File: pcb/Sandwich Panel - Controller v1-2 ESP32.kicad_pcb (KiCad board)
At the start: 2 copper layers, 140 x 50 mm, 28 parts, among them J1 Conn_01x02_Male, J2 Conn_01x02_Male, J4 Conn_01x04, J5 USB_C_Receptacle_USB2.0, U1 ESP32-S3-MINI-1-N8, U2 SPX3819M5-L-3-3

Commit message: Old zones don't seem to be removable, will edit the text file next, wish me luck
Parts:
- removed H4, H5, H6, H7, H8: Mousebites, Pancake:Mousebites_03
- removed J1, J2: Conn_01x02_Male, Pancake:Panel_Connector 02
- removed J4: Conn_01x04, Pancake:I2C Breakout Pads
- added H3: Mousebites, Pancake:Mousebites_03, F.Cu at (33.5, 64.8)
- added H3: Mousebites, Pancake:Mousebites_03, F.Cu at (153.0, 95.2)
- added H3: Mousebites, Pancake:Mousebites_03, F.Cu at (35.0, 144.2)
- added H3: Mousebites, Pancake:Mousebites_03, F.Cu at (153.0, 50.2)
- added H3: Mousebites, Pancake:Mousebites_03, F.Cu at (152.0, 144.2)
- added H3: Mousebites, Pancake:Mousebites_03, F.Cu at (152.0, 116.8)
- added H3: Mousebites, Pancake:Mousebites_03, F.Cu at (34.0, 116.2)
- added H3: Mousebites, Pancake:Mousebites_03, F.Cu at (33.5, 95.8)
- added H3: Mousebites, Pancake:Mousebites_03, F.Cu at (153.0, 64.8)
- added H3: Mousebites, Pancake:Mousebites_03, F.Cu at (151.5, 80.2)
- added H3: Mousebites, Pancake:Mousebites_03, F.Cu at (34.0, 80.8)
- moved H1 220.5 mm to (157.5, 45.0)
- moved H3 117.6 mm to (33.5, 50.2)
- moved U1 114.6 mm to (138.9, 34.0)
- moved TP2 111.9 mm to (135.0, 43.0)
- moved TP3 111.9 mm to (136.5, 43.0)
- moved TP4 111.9 mm to (138.0, 43.0)
- moved TP5 111.9 mm to (139.5, 43.0)
- moved TP6 111.9 mm to (141.0, 43.0)
- moved TP7 111.9 mm to (142.5, 43.0)
- moved C1 110.9 mm to (122.5, 30.0)
- moved C2 110.9 mm to (122.5, 38.7)
- moved C3 110.9 mm to (118.0, 34.4)
- moved R3 110.9 mm to (117.9, 30.1)
- moved TP1 110.9 mm to (126.0, 31.6)
- moved U2 110.9 mm to (122.5, 34.4)
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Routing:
- net +5V: track 133.6 -> 0.00 mm, vias 6 -> 2
- net 3.3V: track 110.3 -> 0.00 mm
- net SDA: track 100.8 -> 0.00 mm, vias 2 -> 1
- net SCL: track 98.8 -> 0.00 mm, vias 2 -> 1
- net Net-(H1-Pad1): track 95.7 -> 0.00 mm
- net Net-(H2-Pad1): track 36.8 -> 0.00 mm
- net D-: track 36.6 -> 0.00 mm
- net D+: track 34.7 -> 0.00 mm
- net Net-(C3-Pad1): track 30.2 -> 0.00 mm
- net DOUT: track 24.8 -> 0.00 mm, vias 2 -> 0
- net GND: track 16.0 -> 0.00 mm, vias 9 -> 4
- net Net-(J5-PadA5): track 11.1 -> 0.00 mm
- net Net-(J5-PadB5): track 7.37 -> 0.00 mm
- net Net-(U1-Pad26): track 4.77 -> 0.00 mm
- net Net-(U1-Pad30): track 4.62 -> 0.00 mm
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- added copper zone on F.Cu, net +5V
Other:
- board size 140 x 50 mm -> 140.5 x 160.6 mm
- board text added: "Controller v1-4"
- board text added: "PancakeLegend et al 2024"
- board text removed: "Controller v1-3"
- board text removed: "JLCJLCJLCJLC"
- board text removed: "PancakeLegend 2023"

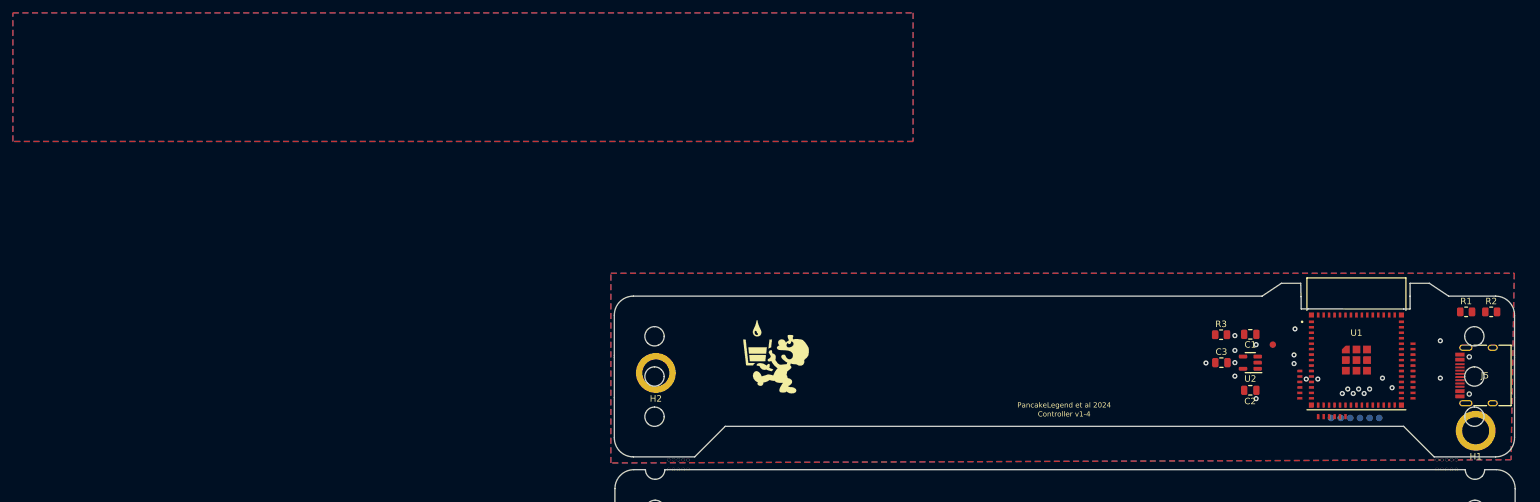
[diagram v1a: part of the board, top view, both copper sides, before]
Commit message: Successful removal of stray zones (manually)
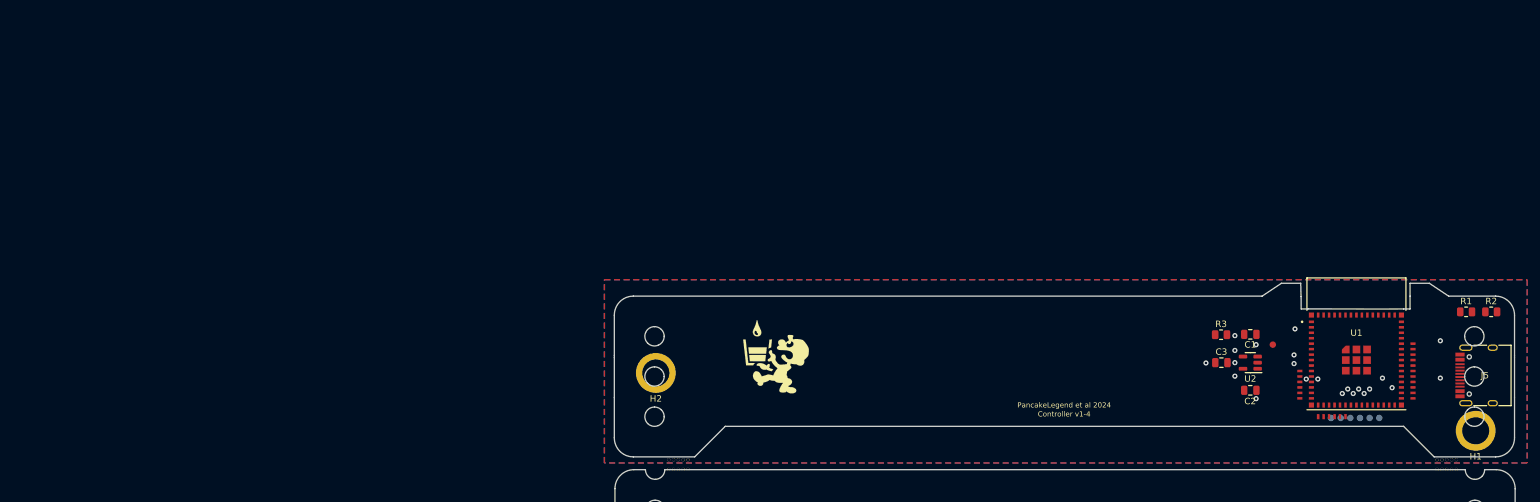
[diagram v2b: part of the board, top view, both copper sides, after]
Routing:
- removed copper zone on F.Cu, net GND
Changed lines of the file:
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@@
 			(pinfunction "GND")
 			(pintype "power_in")
-			(zone_connect 0)
 			(options
 				(clearance outline)
@@
 			(pintype "power_in")
 		)
-		(zone
-			(net 0)
-			(net_name "")
-			(layer "F.Cu")
-			(hatch full 0.508)
-			(connect_pads
-				(clearance 0)
-			)
-			(min_thickness 0.01)
-			(filled_areas_thickness no)
-			(keepout
-				(tracks not_allowed)
-				(vias not_allowed)
-				(pads not_allowed)
-				(copperpour not_allowed)
-				(footprints allowed)
-			)
-			(fill
-				(thermal_gap 0.508)
-				(thermal_bridge_width 0.508)
-			)
-			(polygon
-				(pts
-					(xy 131.25 21.225) (xy 146.65 21.225) (xy 146.65 26.275) (xy 131.25 26.275)
-				)
-			)
-		)
-		(zone
-			(net 0)
-			(net_name "")
-			(layers "*.Cu")
-			(hatch full 0.508)
-			(connect_pads
-				(clearance 0)
-			)
-			(min_thickness 0.01)
-			(filled_areas_thickness no)
-			(keepout
-				(tracks allowed)
-				(vias not_allowed)
-				(pads allowed)
-				(copperpour allowed)
-				(footprints allowed)
-			)
-			(fill
-				(thermal_gap 0.508)
-				(thermal_bridge_width 0.508)
-			)
-			(polygon
-				(pts
-					(xy 131.25 21.225) (xy 146.65 21.225) (xy 146.65 26.275) (xy 131.25 26.275)
-				)
-			)
-		)
-		(zone
-			(net 0)
-			(net_name "")
-			(layer "B.Cu")
-			(hatch full 0.508)
-			(connect_pads
-				(clearance 0)
-			)
-			(min_thickness 0.01)
-			(filled_areas_thickness no)
-			(keepout
-				(tracks not_allowed)
-				(vias not_allowed)
-				(pads not_allowed)
-				(copperpour not_allowed)
-				(footprints allowed)
-			)
-			(fill
-				(thermal_gap 0.508)
-				(thermal_bridge_width 0.508)
-			)
-			(polygon
-				(pts
-					(xy 131.25 21.225) (xy 146.65 21.225) (xy 146.65 26.275) (xy 131.25 26.275)
-				)
-			)
-		)
 		(model "C:/Users/ocd/OneDrive/KiCAD/3D Models/ESP32-S3-MINI-1-N8.step"
 			(offset
@@
 	)
 	(zone
-		(net 1)
-		(net_name "GND")
-		(locked yes)
-		(layer "F.Cu")
-		(hatch edge 0.508)
-		(connect_pads
-			(clearance 0.5)
-		)
-		(min_thickness 0.254)
-		(filled_areas_thickness no)
-		(fill yes
-			(thermal_gap 0.508)
-			(thermal_bridge_width 0.508)
-		)
-		(polygon
-			(pts
-				(xy 70 0) (xy -70 0) (xy -70 -20) (xy 70 -20)
-			)
-		)
-	)
-	(zone
 		(net 4)
 		(net_name "+5V")
 		(layer "F.Cu")
 		(hatch edge 0.5)
-		(priority 1)
 		(connect_pads
 			(clearance 0)
@@
 		(polygon
 			(pts
-				(xy 23 20.5) (xy 163.5 20.5) (xy 163 49.5) (xy 23 50)
+				(xy 165.5 21.5) (xy 165.5 50) (xy 22 50) (xy 22 21.5)
 			)
 		)
@@
 		(layer "B.Cu")
 		(hatch edge 0.5)
-		(priority 2)
 		(connect_pads
 			(clearance 0)
@@
 		(polygon
 			(pts
-				(xy 23 20.5) (xy 163.5 20.5) (xy 163 49.5) (xy 23 50)
-			)
-		)
-	)
-	(zone
-		(net 1)
-		(net_name "GND")
-		(locked yes)
-		(layer "B.Cu")
-		(hatch edge 0.508)
-		(connect_pads
-			(clearance 0.5)
-		)
-		(min_thickness 0.254)
-		(filled_areas_thickness no)
-		(fill yes
-			(thermal_gap 0.508)
-			(thermal_bridge_width 0.508)
-		)
-		(polygon
-			(pts
-				(xy 70 0) (xy -70 0) (xy -70 -20) (xy 70 -20)
+				(xy 165.5 21.5) (xy 165.5 50) (xy 22 50) (xy 22 21.5)
 			)
 		)

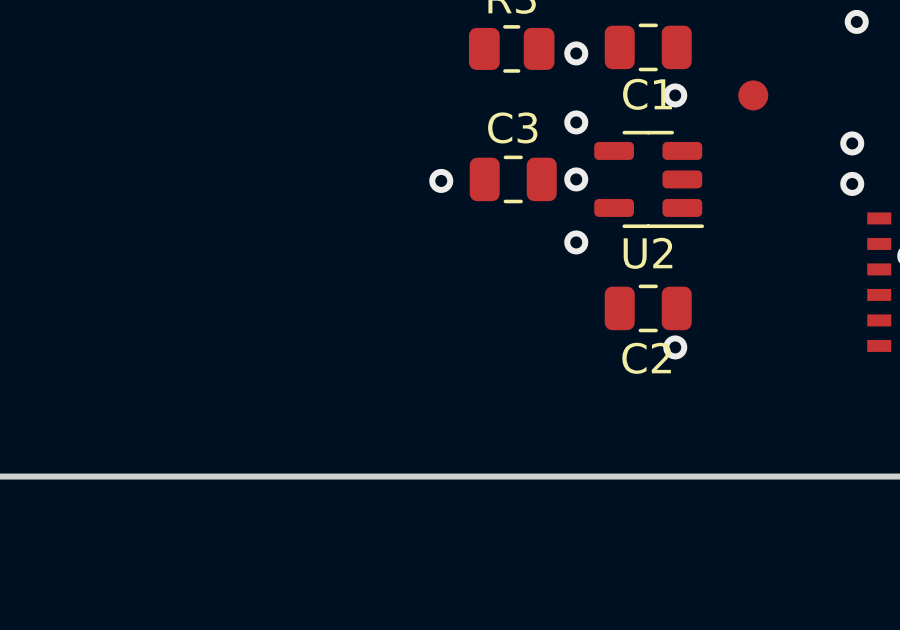
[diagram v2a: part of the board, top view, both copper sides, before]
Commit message: Imported SMD microphone, a bunch of footprints are missing (Pancake library)
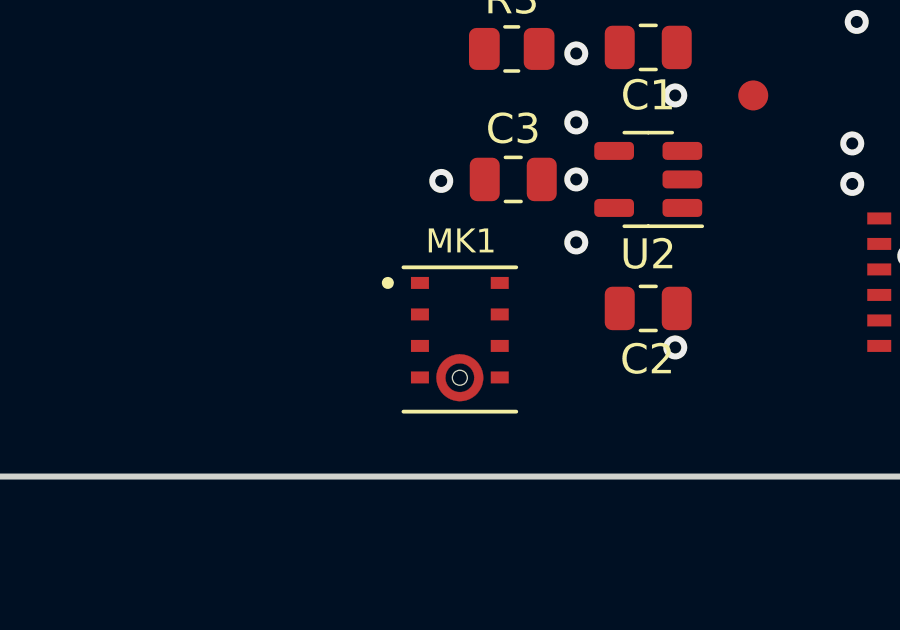
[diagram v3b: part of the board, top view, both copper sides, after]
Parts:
- added MK1: INMP441, inmp441:MIC_INMP441, F.Cu at (116.2, 39.7)
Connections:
- U1 pad 15: unconnected-(U1-Pad15) -> Net-(MK1-SD)
- U1 pad 16: unconnected-(U1-Pad16) -> Net-(MK1-SCK)
- U1 pad 17: unconnected-(U1-Pad17) -> Net-(MK1-WS)
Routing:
- net Net-(J1-Pad1): vias 1 -> 0
- net (no net): vias 0 -> 1

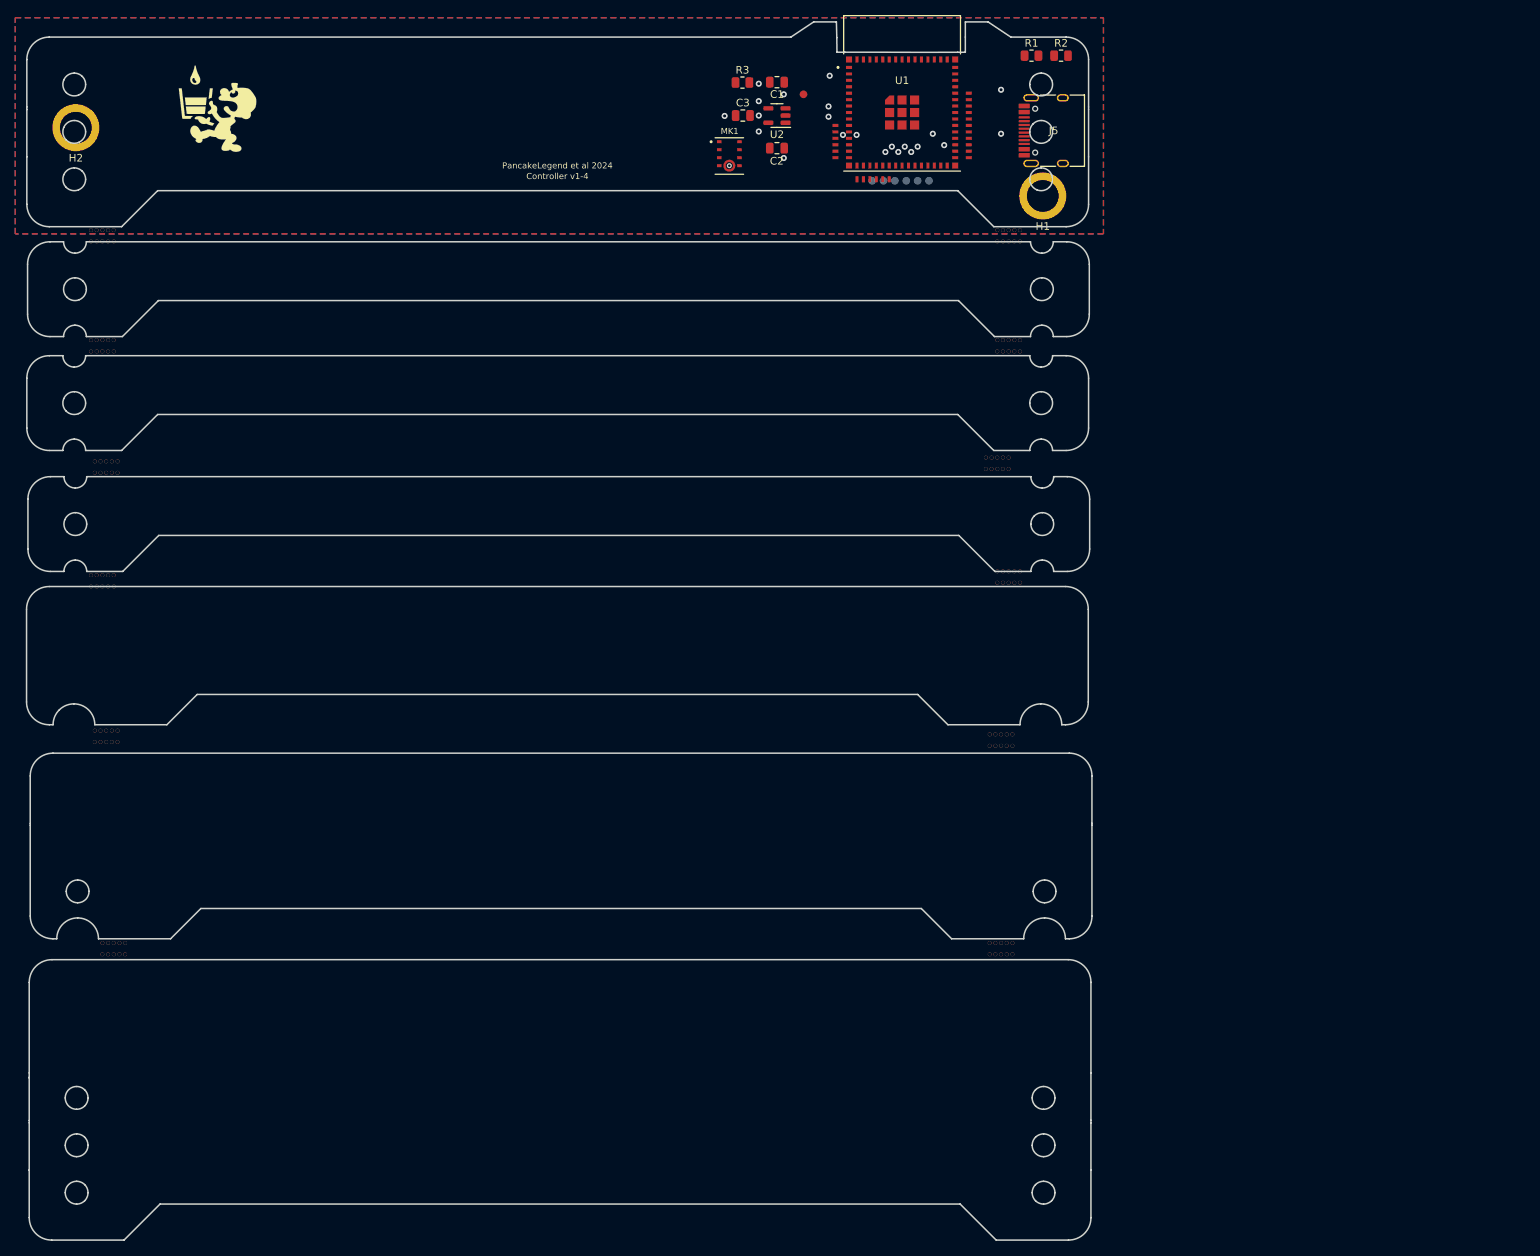
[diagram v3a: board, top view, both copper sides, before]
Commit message: New Edge.Cuts applied
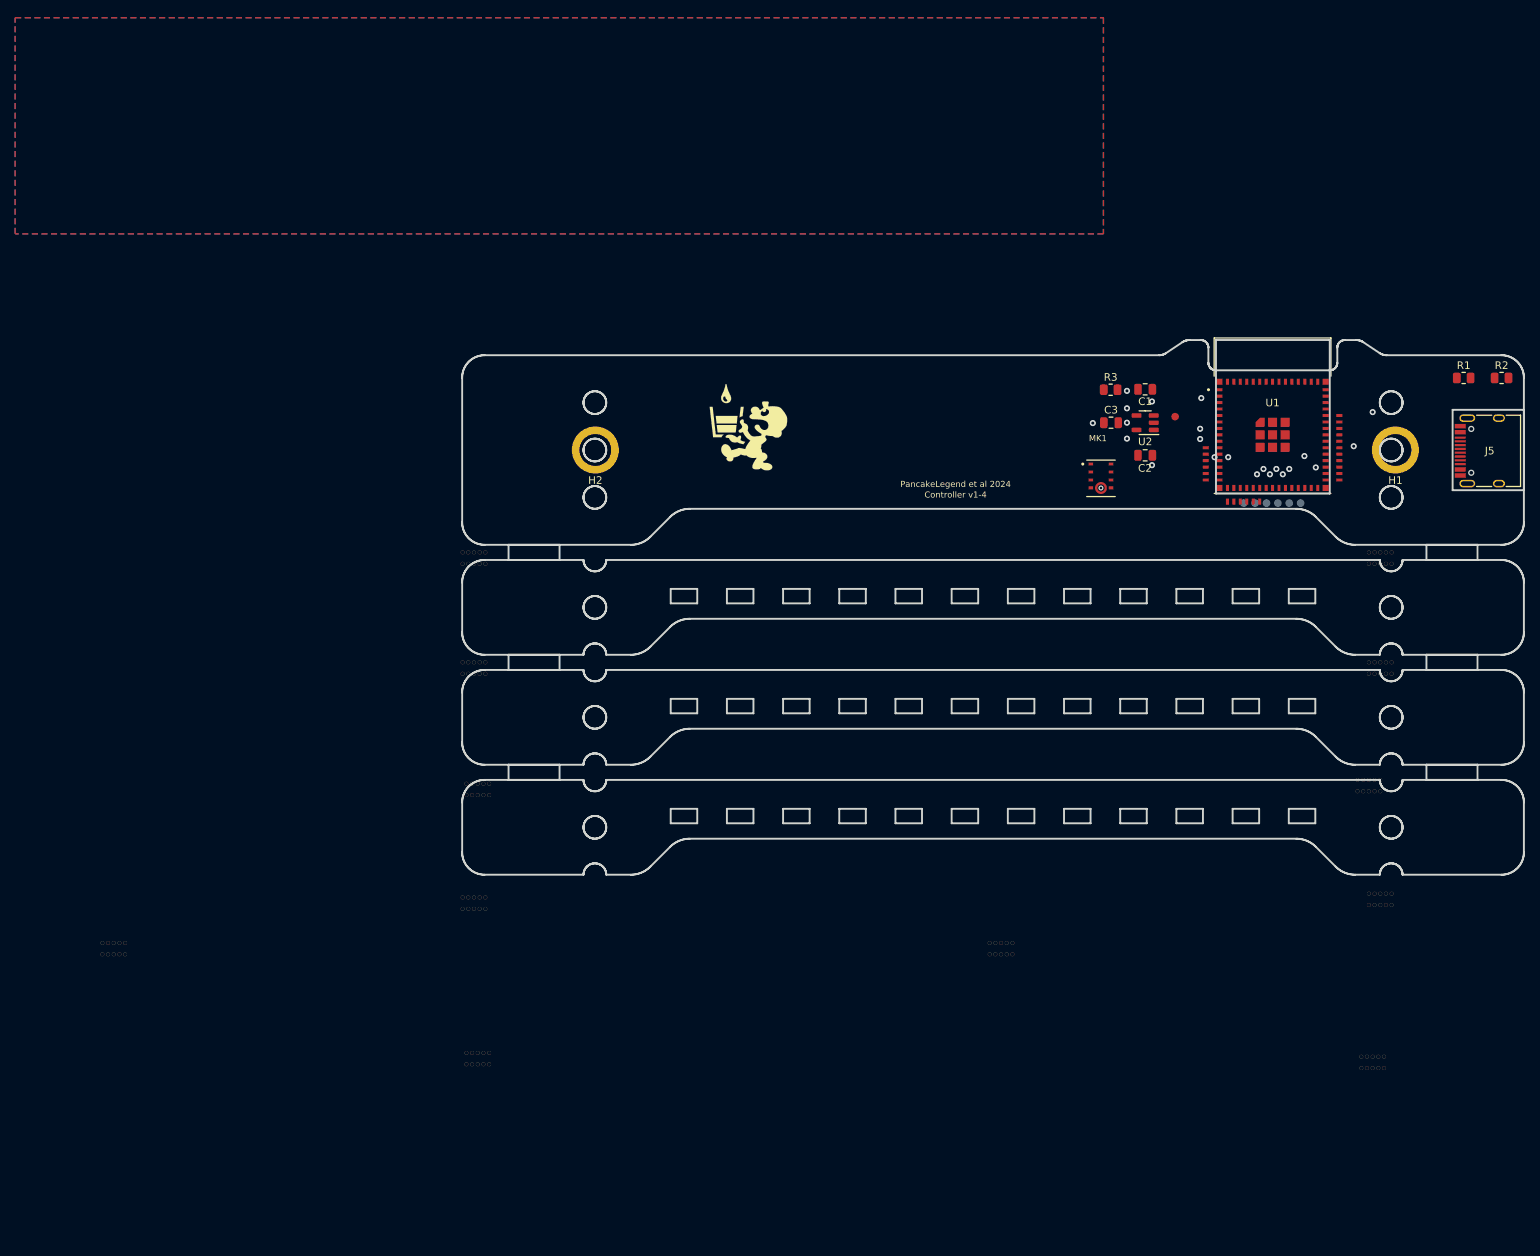
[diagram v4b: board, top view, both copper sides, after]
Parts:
- moved H9 81.6 mm to (118.5, 75.5)
- moved H2 80.6 mm to (98.5, 78.5)
- moved R2 72.0 mm to (218.0, 69.0)
- moved J5 71.3 mm to (216.6, 78.6)
- moved R1 71.1 mm to (213.0, 69.0)
- moved H3 64.9 mm to (82.5, 92.8)
- moved H3 64.9 mm to (82.5, 107.2)
- moved H3 64.9 mm to (202.0, 137.8)
- moved H3 64.9 mm to (202.0, 92.8)
- moved H3 64.9 mm to (201.0, 159.2)
- moved H3 64.9 mm to (83.0, 158.8)
- moved H3 64.9 mm to (82.5, 138.2)
- moved H3 64.9 mm to (202.0, 107.2)
- moved H3 64.9 mm to (200.5, 122.8)
- moved H3 64.9 mm to (83.0, 123.2)
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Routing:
- net Net-(U1-IO2): vias 1 -> 2
- net (no net): vias 1 -> 0
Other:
- board size 140.5 x 160.6 mm -> 140 x 70.5 mm
